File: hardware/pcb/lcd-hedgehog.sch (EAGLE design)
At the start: 34 parts

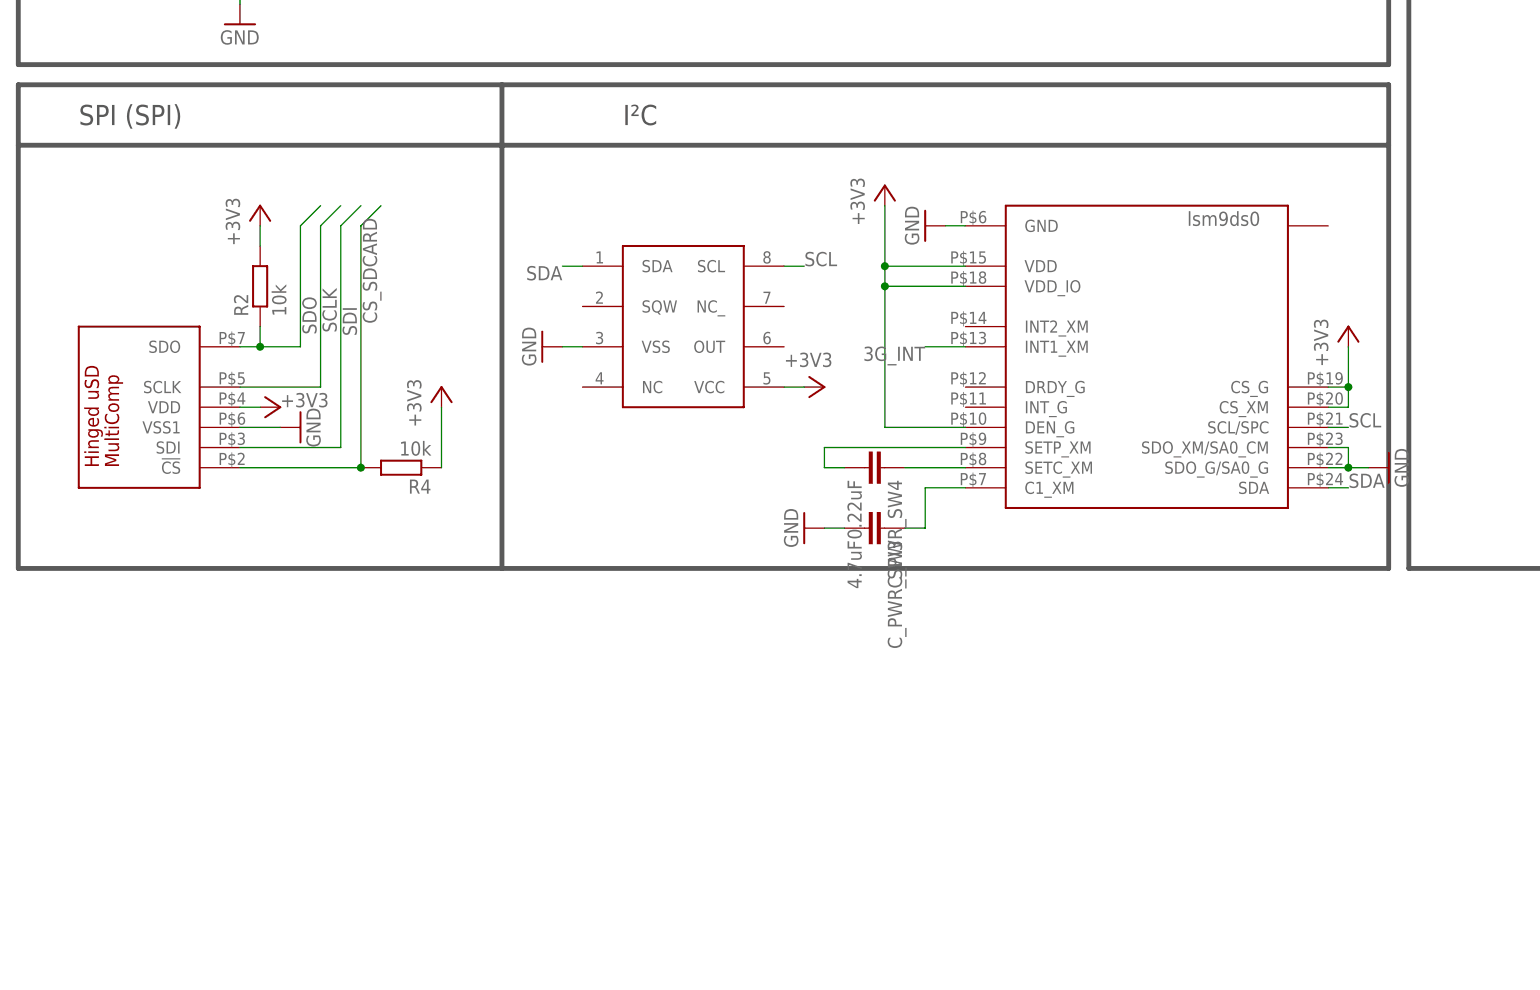
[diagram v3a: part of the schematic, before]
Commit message: added Grid Eye
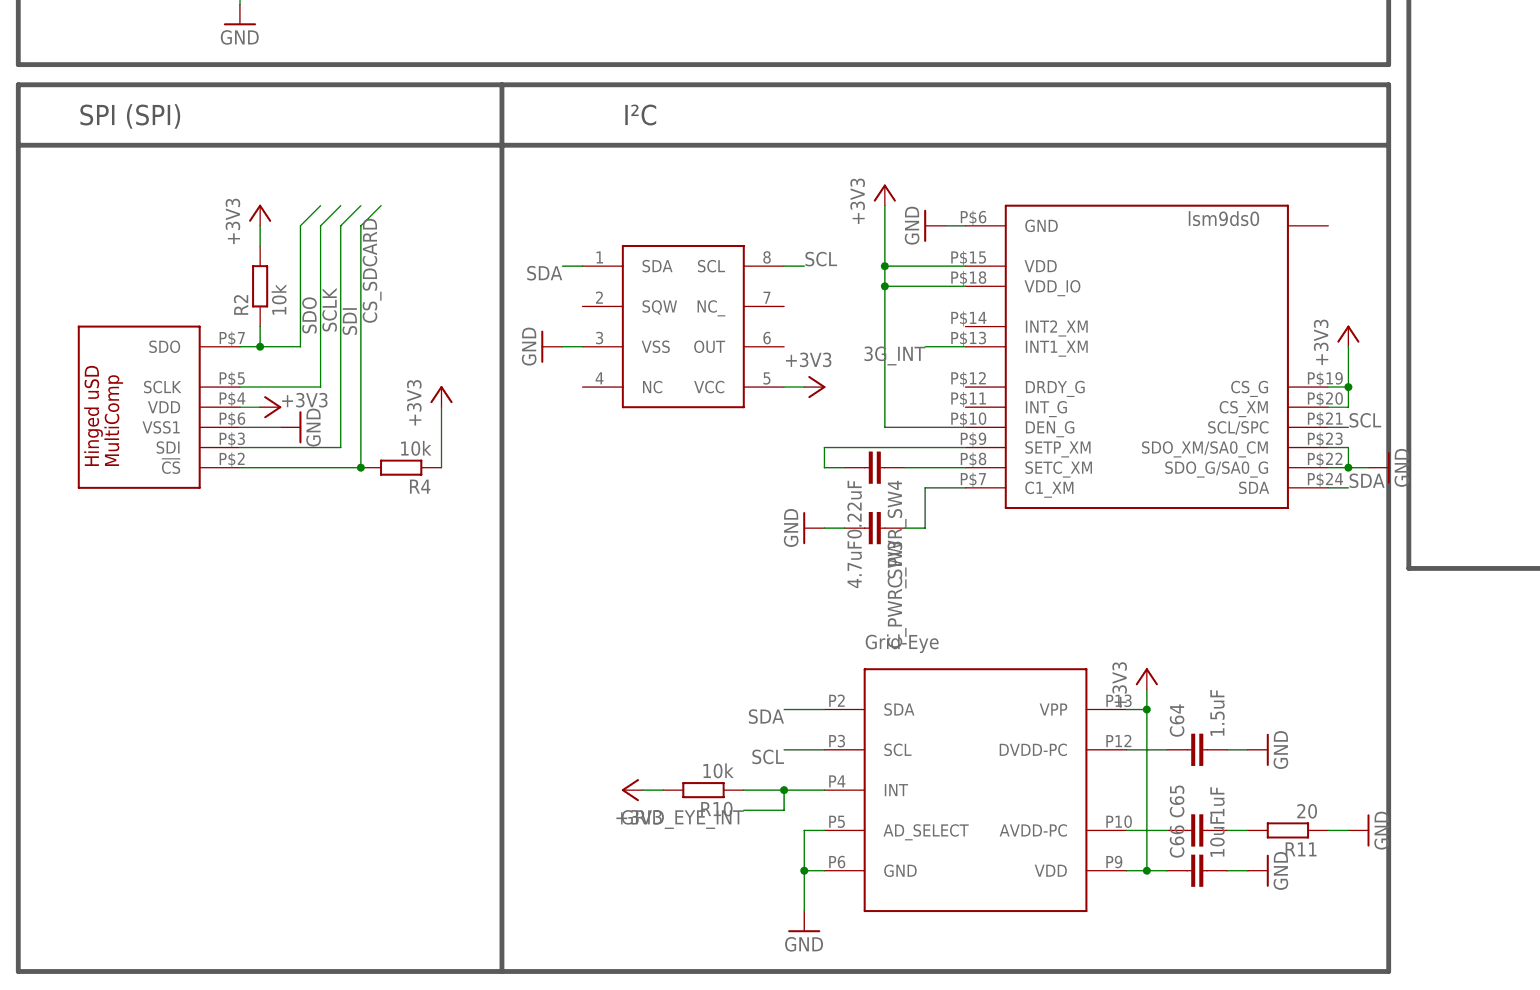
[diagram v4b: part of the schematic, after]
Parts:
- added C64: 1.5uF, rcl:C-EUC0805K
- added C65: 1uF, rcl:C-EUC0805K
- added C66: 10uF, rcl:C-EUC0805K
- added R10: 10k, rcl:R-EU_R0603
- added R11: 20, rcl:R-EU_R0603
- added U$2: GRID-EYE, HedgehogLib:GRID-EYE
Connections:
- new net GRID_EYE_INT: R10.1, U$2.INT
- new net N$12: C64.1, U$2.DVDD-PC
- new net N$13: C65.1, U$2.AVDD-PC
- new net N$14: C65.2, R11.2
- net +3V3: now also C66.1, R10.2, U$2.VDD, U$2.VPP
- net GND: now also C64.2, C66.2, R11.1, U$2.AD_SELECT, U$2.GND
- net SCL: now also U$2.SCL
- net SDA: now also U$2.SDA
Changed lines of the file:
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@@
 <?xml version="1.0" encoding="utf-8"?>
 <!DOCTYPE eagle SYSTEM "eagle.dtd">
-<eagle version="6.3">
+<eagle version="6.5.0">
 <drawing>
 <settings>
@@
 <part name="R9" library="rcl" deviceset="R-EU_" device="R0603" value="3k3"/>
 <part name="+3V15" library="supply1" deviceset="+3V3" device=""/>
+<part name="U$2" library="HedgehogLib" deviceset="GRID-EYE" device=""/>
+<part name="+3V16" library="supply1" deviceset="+3V3" device=""/>
+<part name="+3V18" library="supply1" deviceset="+3V3" device=""/>
+<part name="R10" library="rcl" deviceset="R-EU_" device="R0603" value="10k"/>
+<part name="GND28" library="supply1" deviceset="GND" device=""/>
+<part name="C64" library="rcl" deviceset="C-EU" device="C0805K" value="1.5uF"/>
+<part name="C65" library="rcl" deviceset="C-EU" device="C0805K" value="1uF"/>
+<part name="R11" library="rcl" deviceset="R-EU_" device="R0603" value="20"/>
+<part name="GND29" library="supply1" deviceset="GND" device=""/>
+<part name="GND30" library="supply1" deviceset="GND" device=""/>
+<part name="GND32" library="supply1" deviceset="GND" device=""/>
+<part name="C66" library="rcl" deviceset="C-EU" device="C0805K" value="10uF"/>
 </parts>
 <sheets>
@@
 <wire x1="175.26" y1="121.92" x2="175.26" y2="66.04" width="0.6096" layer="97"/>
 <wire x1="2.54" y1="129.54" x2="2.54" y2="121.92" width="0.6096" layer="97"/>
-<wire x1="2.54" y1="55.88" x2="2.54" y2="2.54" width="0.6096" layer="97"/>
+<wire x1="2.54" y1="55.88" x2="2.54" y2="-48.26" width="0.6096" layer="97"/>
 <wire x1="175.26" y1="63.5" x2="63.5" y2="63.5" width="0.6096" layer="97"/>
 <wire x1="63.5" y1="63.5" x2="2.54" y2="63.5" width="0.6096" layer="97"/>
@@
 <wire x1="63.5" y1="55.88" x2="2.54" y2="55.88" width="0.6096" layer="97"/>
 <wire x1="175.26" y1="63.5" x2="175.26" y2="55.88" width="0.6096" layer="97"/>
-<wire x1="175.26" y1="55.88" x2="175.26" y2="2.54" width="0.6096" layer="97"/>
-<wire x1="2.54" y1="2.54" x2="63.5" y2="2.54" width="0.6096" layer="97"/>
-<wire x1="63.5" y1="2.54" x2="175.26" y2="2.54" width="0.6096" layer="97"/>
+<wire x1="175.26" y1="55.88" x2="175.26" y2="-48.26" width="0.6096" layer="97"/>
+<wire x1="2.54" y1="-48.26" x2="63.5" y2="-48.26" width="0.6096" layer="97"/>
+<wire x1="63.5" y1="-48.26" x2="175.26" y2="-48.26" width="0.6096" layer="97"/>
 <wire x1="2.54" y1="63.5" x2="2.54" y2="55.88" width="0.6096" layer="97"/>
 <wire x1="177.8" y1="129.54" x2="177.8" y2="121.92" width="0.6096" layer="97"/>
@@
 <text x="6.604" y="241.554" size="2.54" layer="97">Bluetooth</text>
 <text x="78.74" y="58.42" size="2.54" layer="97">I²C</text>
-<wire x1="63.5" y1="55.88" x2="63.5" y2="2.54" width="0.6096" layer="97"/>
+<wire x1="63.5" y1="55.88" x2="63.5" y2="-48.26" width="0.6096" layer="97"/>
 <wire x1="63.5" y1="63.5" x2="63.5" y2="55.88" width="0.6096" layer="97"/>
 </plain>
@@
 <instance part="R9" gate="G$1" x="269.24" y="139.7" rot="R180"/>
 <instance part="+3V15" gate="G$1" x="259.08" y="139.7" rot="R90"/>
+<instance part="U$2" gate="G$1" x="124.46" y="-25.4"/>
+<instance part="+3V16" gate="G$1" x="144.78" y="-10.16"/>
+<instance part="+3V18" gate="G$1" x="78.74" y="-25.4" rot="R90"/>
+<instance part="R10" gate="G$1" x="88.9" y="-25.4" rot="R180"/>
+<instance part="GND28" gate="1" x="101.6" y="-43.18"/>
+<instance part="C64" gate="G$1" x="149.86" y="-20.32" rot="R90"/>
+<instance part="C65" gate="G$1" x="149.86" y="-30.48" rot="R90"/>
+<instance part="R11" gate="G$1" x="162.56" y="-30.48" rot="R180"/>
+<instance part="GND29" gate="1" x="172.72" y="-30.48" rot="R90"/>
+<instance part="GND30" gate="1" x="160.02" y="-20.32" rot="R90"/>
+<instance part="GND32" gate="1" x="160.02" y="-35.56" rot="R90"/>
+<instance part="C66" gate="G$1" x="149.86" y="-35.56" rot="R90"/>
 </instances>
 <busses>
@@
 <wire x1="180.34" y1="147.32" x2="180.34" y2="149.86" width="0.1524" layer="91"/>
 </segment>
+<segment>
+<pinref part="U$2" gate="G$1" pin="AD_SELECT"/>
+<pinref part="GND28" gate="1" pin="GND"/>
+<wire x1="104.14" y1="-30.48" x2="101.6" y2="-30.48" width="0.1524" layer="91"/>
+<wire x1="101.6" y1="-30.48" x2="101.6" y2="-35.56" width="0.1524" layer="91"/>
+<pinref part="U$2" gate="G$1" pin="GND"/>
+<wire x1="101.6" y1="-35.56" x2="101.6" y2="-40.64" width="0.1524" layer="91"/>
+<wire x1="104.14" y1="-35.56" x2="101.6" y2="-35.56" width="0.1524" layer="91"/>
+<junction x="101.6" y="-35.56"/>
+</segment>
+<segment>
+<pinref part="R11" gate="G$1" pin="1"/>
+<pinref part="GND29" gate="1" pin="GND"/>
+<wire x1="170.18" y1="-30.48" x2="167.64" y2="-30.48" width="0.1524" layer="91"/>
+</segment>
+<segment>
+<pinref part="C64" gate="G$1" pin="2"/>
+<pinref part="GND30" gate="1" pin="GND"/>
+<wire x1="157.48" y1="-20.32" x2="154.94" y2="-20.32" width="0.1524" layer="91"/>
+</segment>
+<segment>
+<pinref part="C66" gate="G$1" pin="2"/>
+<pinref part="GND32" gate="1" pin="GND"/>
+<wire x1="154.94" y1="-35.56" x2="157.48" y2="-35.56" width="0.1524" layer="91"/>
+</segment>
 </net>
 <net name="D+" class="0">
@@
 <pinref part="R9" gate="G$1" pin="2"/>
 <wire x1="261.62" y1="139.7" x2="264.16" y2="139.7" width="0.1524" layer="91"/>
+</segment>
+<segment>
+<pinref part="+3V18" gate="G$1" pin="+3V3"/>
+<pinref part="R10" gate="G$1" pin="2"/>
+<wire x1="81.28" y1="-25.4" x2="83.82" y2="-25.4" width="0.1524" layer="91"/>
+</segment>
+<segment>
+<pinref part="U$2" gate="G$1" pin="VPP"/>
+<pinref part="+3V16" gate="G$1" pin="+3V3"/>
+<wire x1="142.24" y1="-15.24" x2="144.78" y2="-15.24" width="0.1524" layer="91"/>
+<wire x1="144.78" y1="-15.24" x2="144.78" y2="-12.7" width="0.1524" layer="91"/>
+<pinref part="C66" gate="G$1" pin="1"/>
+<pinref part="U$2" gate="G$1" pin="VDD"/>
+<wire x1="147.32" y1="-35.56" x2="144.78" y2="-35.56" width="0.1524" layer="91"/>
+<wire x1="144.78" y1="-35.56" x2="142.24" y2="-35.56" width="0.1524" layer="91"/>
+<wire x1="144.78" y1="-15.24" x2="144.78" y2="-35.56" width="0.1524" layer="91"/>
+<junction x="144.78" y="-35.56"/>
+<junction x="144.78" y="-15.24"/>
 </segment>
 </net>
@@
 <label x="279.4" y="139.7" size="1.778" layer="95"/>
 </segment>
+<segment>
+<pinref part="U$2" gate="G$1" pin="SDA"/>
+<wire x1="104.14" y1="-15.24" x2="99.06" y2="-15.24" width="0.1524" layer="91"/>
+<label x="99.06" y="-15.24" size="1.778" layer="95" rot="R180"/>
+</segment>
 </net>
 <net name="SCL" class="0">
@@
 <wire x1="274.32" y1="144.78" x2="279.4" y2="144.78" width="0.1524" layer="91"/>
 <label x="279.4" y="144.78" size="1.778" layer="95"/>
+</segment>
+<segment>
+<pinref part="U$2" gate="G$1" pin="SCL"/>
+<wire x1="104.14" y1="-20.32" x2="99.06" y2="-20.32" width="0.1524" layer="91"/>
+<label x="99.06" y="-20.32" size="1.778" layer="95" rot="R180"/>
 </segment>
 </net>
@@
 </segment>
 </net>
+<net name="GRID_EYE_INT" class="0">
+<segment>
+<pinref part="U$2" gate="G$1" pin="INT"/>
+<pinref part="R10" gate="G$1" pin="1"/>
+<wire x1="104.14" y1="-25.4" x2="99.06" y2="-25.4" width="0.1524" layer="91"/>
+<wire x1="99.06" y1="-25.4" x2="93.98" y2="-25.4" width="0.1524" layer="91"/>
+<wire x1="99.06" y1="-25.4" x2="99.06" y2="-27.94" width="0.1524" layer="91"/>
+<wire x1="99.06" y1="-27.94" x2="93.98" y2="-27.94" width="0.1524" layer="91"/>
+<label x="93.98" y="-27.94" size="1.778" layer="95" rot="R180"/>
+<junction x="99.06" y="-25.4"/>
+</segment>
+</net>
+<net name="N$12" class="0">
+<segment>
+<pinref part="U$2" gate="G$1" pin="DVDD-PC"/>
+<pinref part="C64" gate="G$1" pin="1"/>
+<wire x1="147.32" y1="-20.32" x2="142.24" y2="-20.32" width="0.1524" layer="91"/>
+</segment>
+</net>
+<net name="N$13" class="0">
+<segment>
+<pinref part="U$2" gate="G$1" pin="AVDD-PC"/>
+<pinref part="C65" gate="G$1" pin="1"/>
+<wire x1="147.32" y1="-30.48" x2="142.24" y2="-30.48" width="0.1524" layer="91"/>
+</segment>
+</net>
+<net name="N$14" class="0">
+<segment>
+<pinref part="C65" gate="G$1" pin="2"/>
+<pinref part="R11" gate="G$1" pin="2"/>
+<wire x1="157.48" y1="-30.48" x2="154.94" y2="-30.48" width="0.1524" layer="91"/>
+</segment>
+</net>
